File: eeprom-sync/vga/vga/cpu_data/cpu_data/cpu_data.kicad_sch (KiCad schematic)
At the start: 34 parts, among them J1 Conn_02x06_Odd_Even, J10 Conn_01x03_Female, J11 Conn_01x02_Female, J12 Conn_02x05_Odd_Even, J2 Conn_01x04_Male, J3 Conn_01x04_Female, J4 Conn_01x15_Female, J5 Conn_01x15_Female, J6 Conn_01x08_Female, J7 Conn_02x03_Odd_Even, J8 Conn_02x08_Odd_Even, J9 Conn_01x08_Female, Q1 Q_NMOS_GSD, U1 GAL22V10, U2 74HC14, U3 74LS02, U4 IDT7205L12JG, U5 74LS573

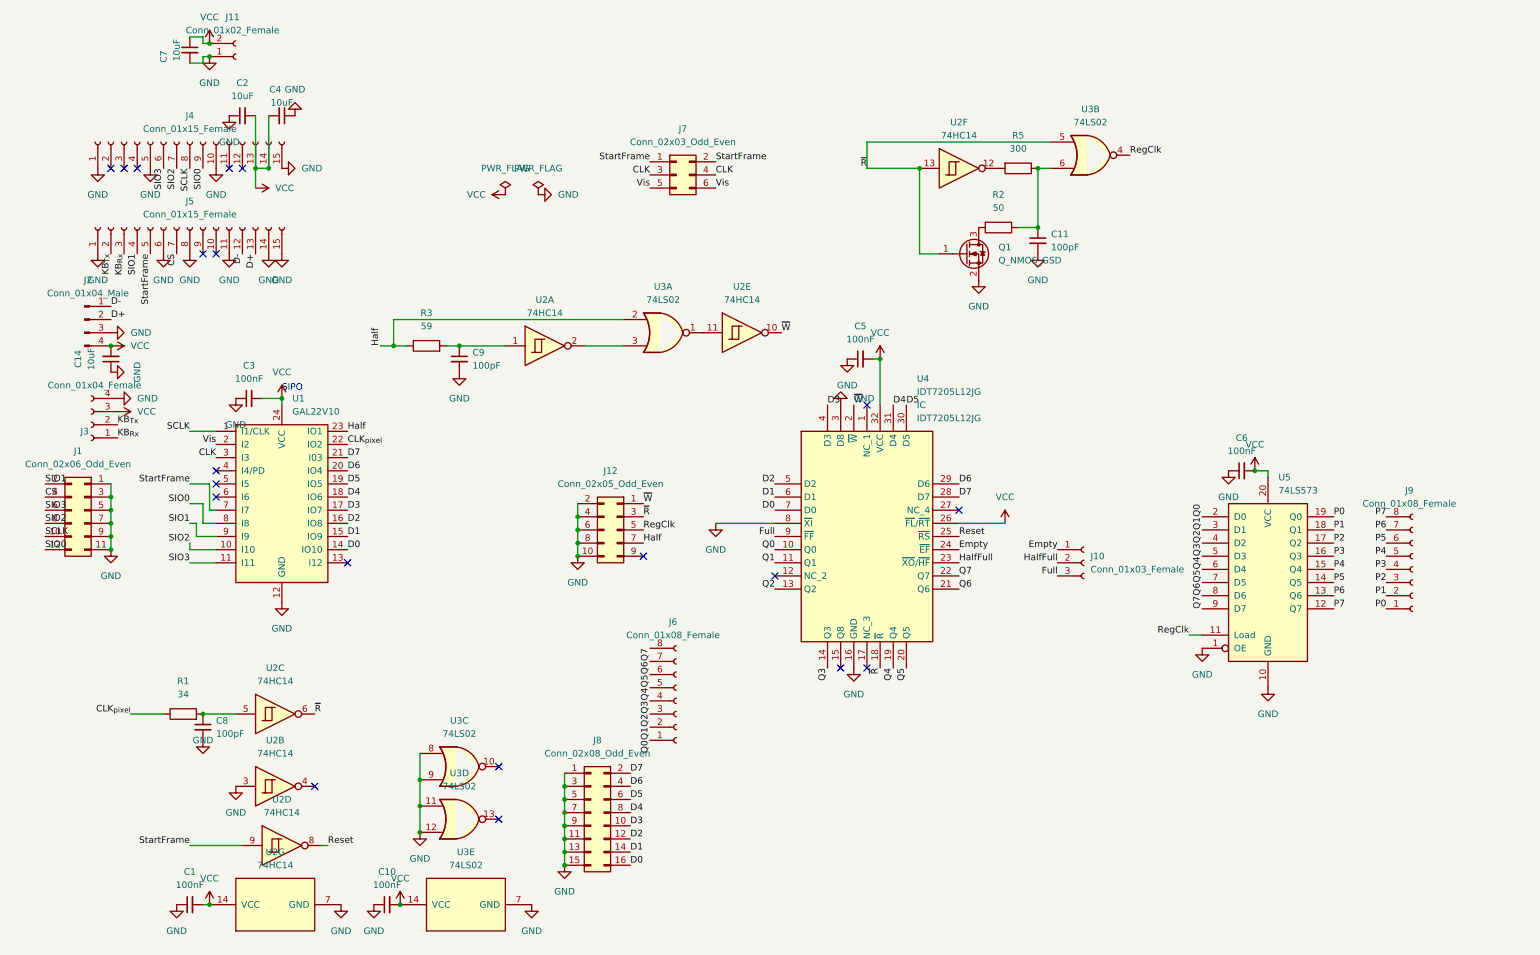
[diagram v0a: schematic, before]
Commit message: added power and pixel indicator LEDs, rearranged and changed some headers for clearance of the GAL, fixed a location issue with a decoup cap
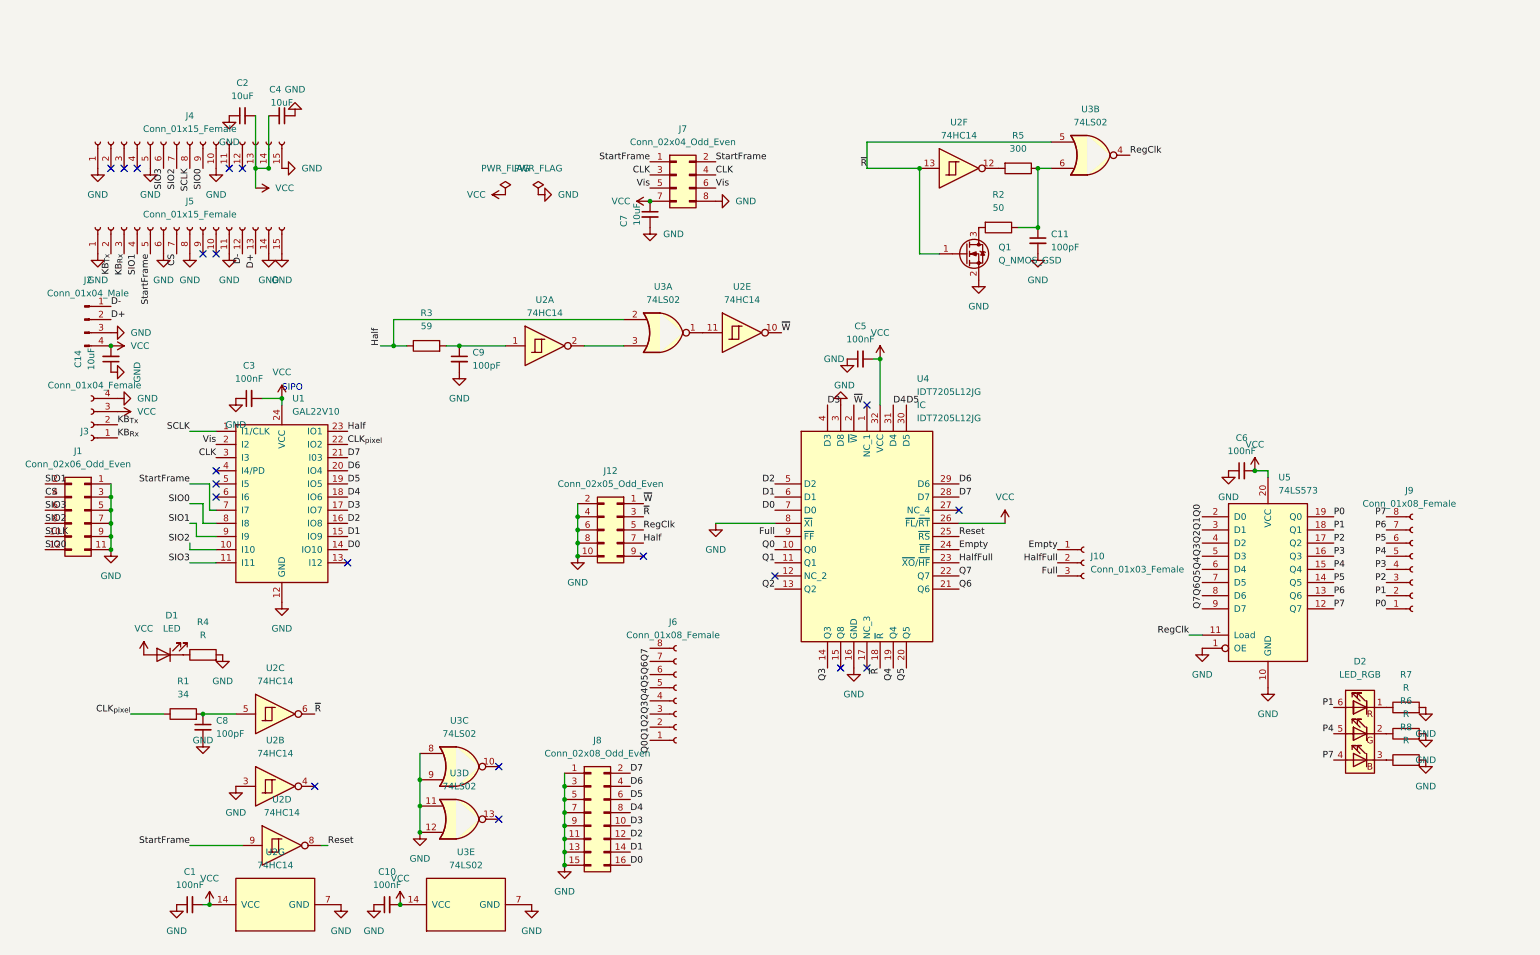
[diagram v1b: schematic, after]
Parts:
- removed J11: Conn_01x02_Female, Connector_PinSocket_2.54mm:PinSocket_1x02_P2.54mm_Vertical, symbol Connector:Conn_01x02_Female
- removed J7: Conn_02x03_Odd_Even, Connector_PinSocket_2.54mm:PinSocket_2x03_P2.54mm_Vertical, symbol Connector_Generic:Conn_02x03_Odd_Even
- added D1: LED, LED_SMD:LED_0805_2012Metric_Pad1.15x1.40mm_HandSolder, symbol Device:LED
- added D2: LED_RGB, LED_SMD:LED_Avago_PLCC6_3x2.8mm, symbol Device:LED_RGB
- added J7: Conn_02x04_Odd_Even, Connector_PinSocket_2.54mm:PinSocket_2x04_P2.54mm_Vertical, symbol Connector_Generic:Conn_02x04_Odd_Even
- added R4, R6, R7, R8: R, Resistor_SMD:R_0805_2012Metric_Pad1.20x1.40mm_HandSolder, symbol Device:R
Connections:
- net CLK: now also J7.3 (Pin_3), J7.4 (Pin_4)
- net GND: now also J7.8 (Pin_8), R4.2, R6.2, R7.2, R8.2
- net P1: now also D2.6 (RA)
- net P4: now also D2.5 (GA)
- net P7: now also D2.4 (BA)
- net StartFrame: now also J7.1 (Pin_1), J7.2 (Pin_2)
- net VCC: now also D1.2 (A), J7.7 (Pin_7)
- net Vis: now also J7.5 (Pin_5), J7.6 (Pin_6)
- new net: D2.3 (BK), R8.1
- new net: D1.1 (K), R4.1
- new net: D2.2 (GK), R6.1
- new net: D2.1 (RK), R7.1
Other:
- moved on the sheet: C7

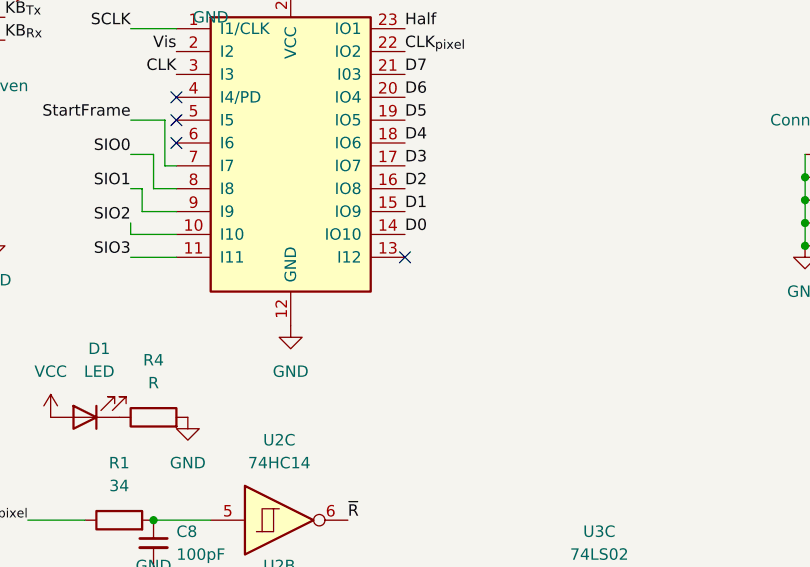
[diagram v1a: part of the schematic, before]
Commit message: gnd-ing the /OE on the gal
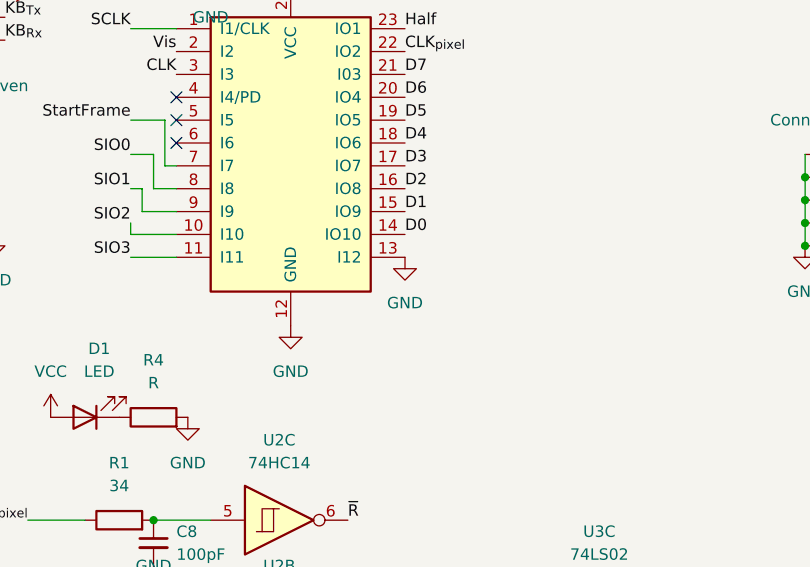
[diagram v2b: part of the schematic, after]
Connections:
- net GND: now also U1.13 (I12)
- no-connect marks 20 -> 19
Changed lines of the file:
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@@
   (no_connect (at 46.99 105.41))
   (no_connect (at 46.99 102.87))
-  (no_connect (at 72.39 118.11))
   (no_connect (at 31.75 41.91))
   (no_connect (at 46.99 58.42))
@@
     (pin "1")
   )
+  (symbol (lib_id "power:GND") (at 72.39 118.11 0) (unit 1)
+    (in_bom yes) (on_board yes) (fields_autoplaced)
+    (property "Reference" "#PWR?" (id 0) (at 72.39 124.46 0)
+      (effects (font (size 1.27 1.27)) hide)
+    )
+    (property "Value" "GND" (id 1) (at 72.39 123.19 0))
+    (property "Footprint" "" (id 2) (at 72.39 118.11 0)
+      (effects (font (size 1.27 1.27)) hide)
+    )
+    (property "Datasheet" "" (id 3) (at 72.39 118.11 0)
+      (effects (font (size 1.27 1.27)) hide)
+    )
+    (pin "1")
+  )
   (symbol (lib_id "power:GND") (at 24.13 41.91 0) (unit 1)
     (in_bom yes) (on_board yes) (fields_autoplaced)
@@
       (reference "#PWR0113") (unit 1) (value "GND") (footprint "")
     )
+    (path "/5d176d2b-4ec8-4c9b-a516-da3798ba757a"
+      (reference "#PWR?") (unit 1) (value "GND") (footprint "")
+    )
     (path "/6d97fa49-1c40-4588-b114-7b816ee2ddf7"
